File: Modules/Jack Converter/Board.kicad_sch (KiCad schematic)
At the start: 39 parts, among them J1 TS_Jack_3.5mm_Sw, J10 TS_Jack_6.35mm_Sw, J100 IDC_02x08, J11 TS_Jack_3.5mm_Sw, J12 TS_Jack_6.35mm_Sw, J13 TS_Jack_3.5mm_Sw, J14 TS_Jack_6.35mm_Sw, J15 TS_Jack_3.5mm_Sw, J16 TS_Jack_6.35mm_Sw, J17 TS_Jack_3.5mm_Sw, J18 TS_Jack_6.35mm_Sw, J19 TS_Jack_3.5mm_Sw, J2 TS_Jack_6.35mm_Sw, J20 TS_Jack_6.35mm_Sw, J21 TS_Jack_3.5mm_Sw, J22 TS_Jack_6.35mm_Sw, J23 TS_Jack_6.35mm, J3 TS_Jack_3.5mm_Sw, J4 TS_Jack_6.35mm_Sw, J5 TS_Jack_3.5mm_Sw, J6 TS_Jack_6.35mm_Sw, J7 TS_Jack_3.5mm_Sw, J8 TS_Jack_6.35mm_Sw, J9 TS_Jack_3.5mm_Sw, SW1 SW_DPDT, SW2 SW_DPDT, SW3 SW_DPDT, SW4 SW_DPDT

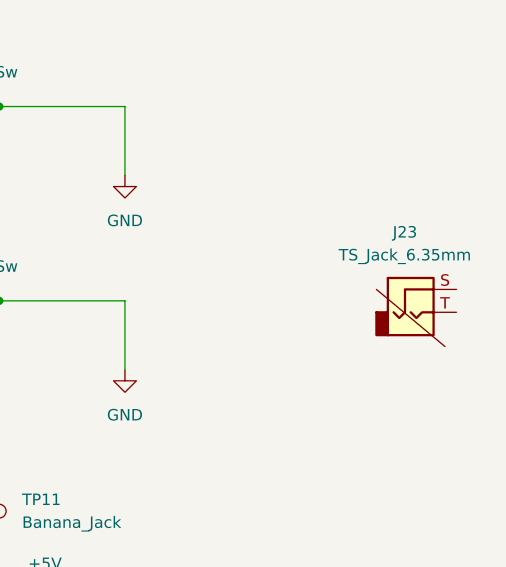
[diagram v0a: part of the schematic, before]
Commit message: Cleaned schematic and downloaded jack mods to footprint library
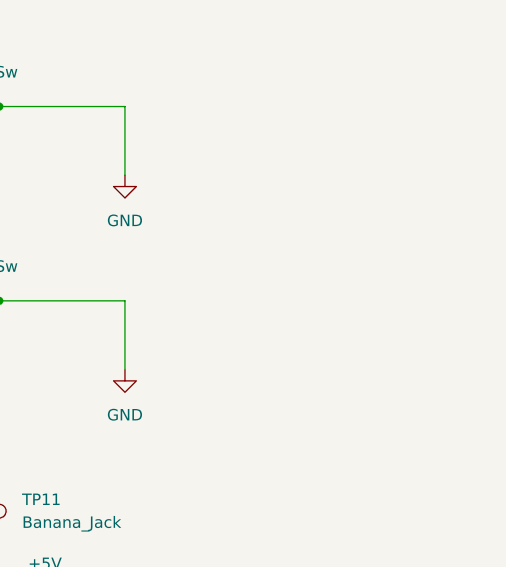
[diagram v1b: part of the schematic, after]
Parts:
- removed J23: TS_Jack_6.35mm, symbol Synth_Stuff:TS_Jack_6.35mm
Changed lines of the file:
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@@
-	)
-	(symbol
-		(lib_id "Synth_Stuff:TS_Jack_6.35mm")
-		(at 251.46 62.23 0)
-		(unit 1)
-		(exclude_from_sim no)
-		(in_bom yes)
-		(on_board yes)
-		(dnp no)
-		(fields_autoplaced yes)
-		(property "Reference" "J23"
-			(at 250.825 53.34 0)
-			(effects
-				(font
-					(size 1.27 1.27)
-				)
-			)
-		)
-		(property "Value" "TS_Jack_6.35mm"
-			(at 250.825 55.88 0)
-			(effects
-				(font
-					(size 1.27 1.27)
-				)
-			)
-		)
-		(property "Footprint" ""
-			(at 251.46 62.23 0)
-			(effects
-				(font
-					(size 1.27 1.27)
-				)
-				(hide yes)
-			)
-		)
-		(property "Datasheet" "~"
-			(at 251.46 62.23 0)
-			(effects
-				(font
-					(size 1.27 1.27)
-				)
-				(hide yes)
-			)
-		)
-		(property "Description" "Audio Jack, 2 Poles (Mono / TS)"
-			(at 251.46 62.23 0)
-			(effects
-				(font
-					(size 1.27 1.27)
-				)
-				(hide yes)
-			)
-		)
-		(pin "T"
-		)
-		(pin "S"
-		)
-		(instances
-			(project "Jack Converter"
-				(path "/b497d75e-0918-4e9c-ae43-36360bc031dc/01b3bf80-fded-40b5-ad81-2678b7ef607a"
-					(reference "J23")
-					(unit 1)
-				)
-			)
-		)
 	)
 	(symbol

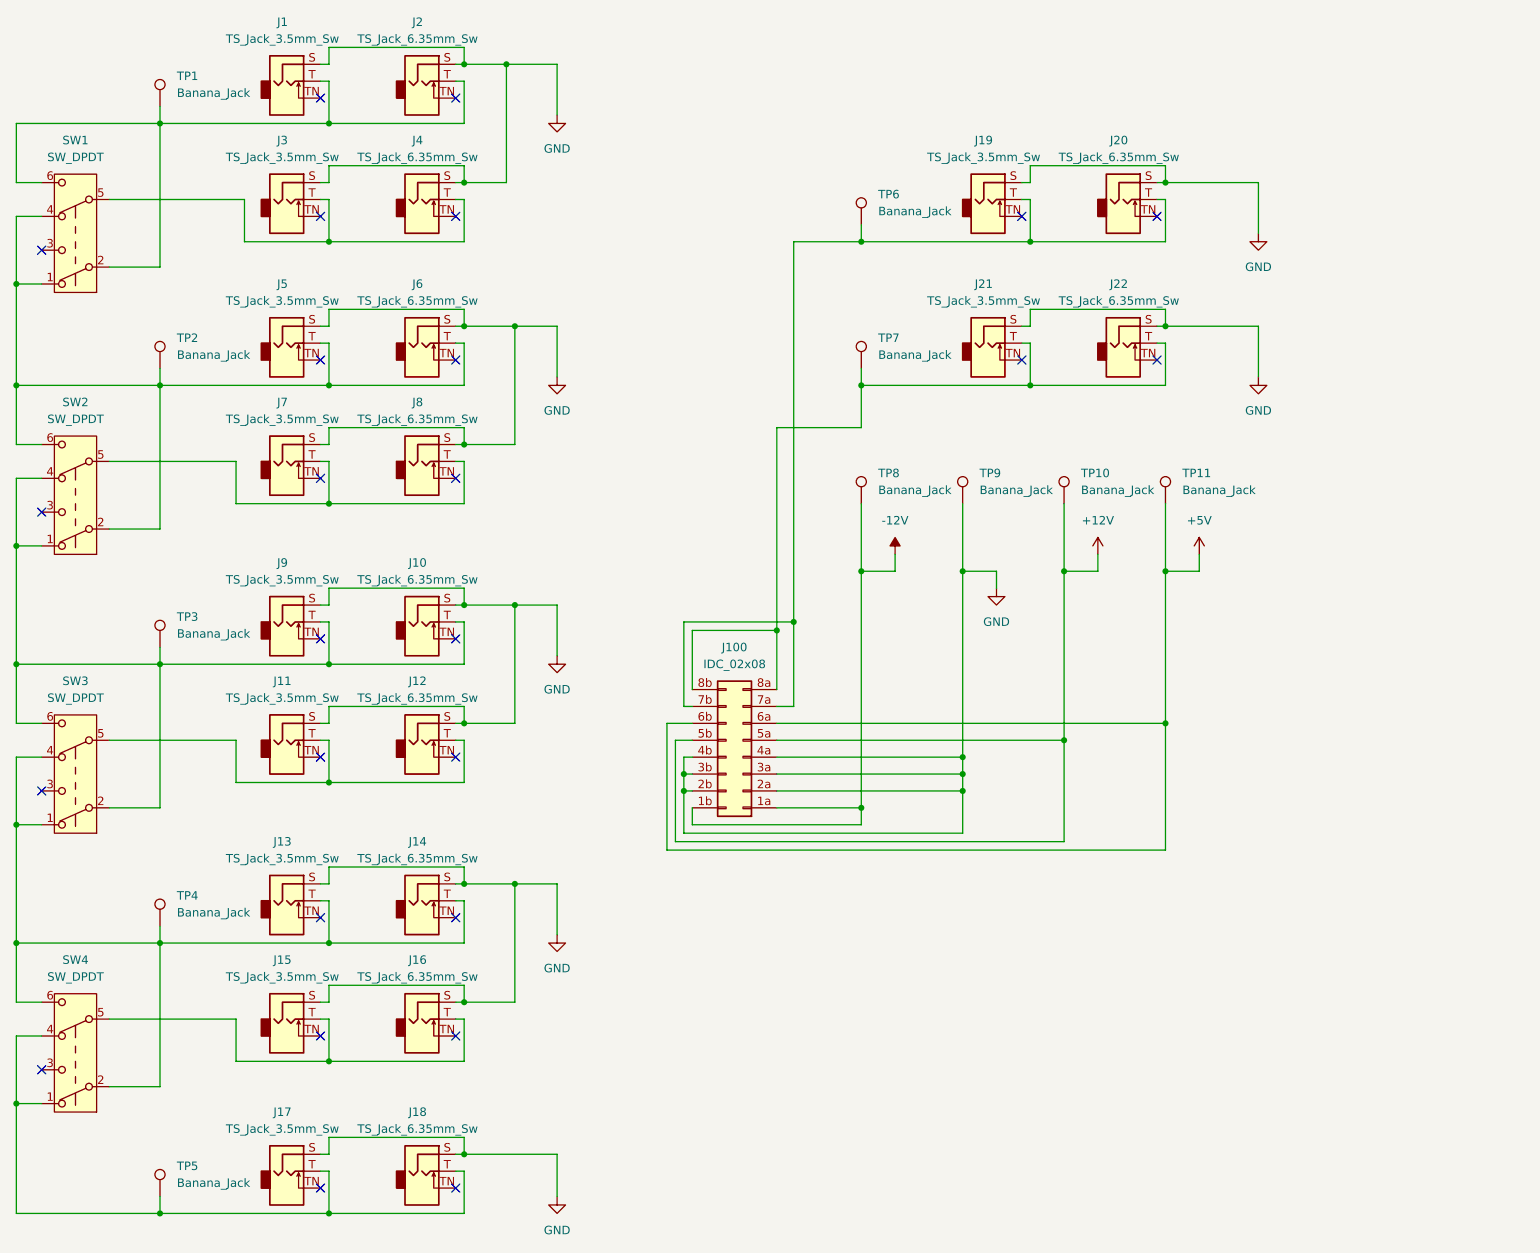
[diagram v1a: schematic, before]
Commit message: Started board PCB creation
Had to remove 2 rows of jacks due to PCB space restriction
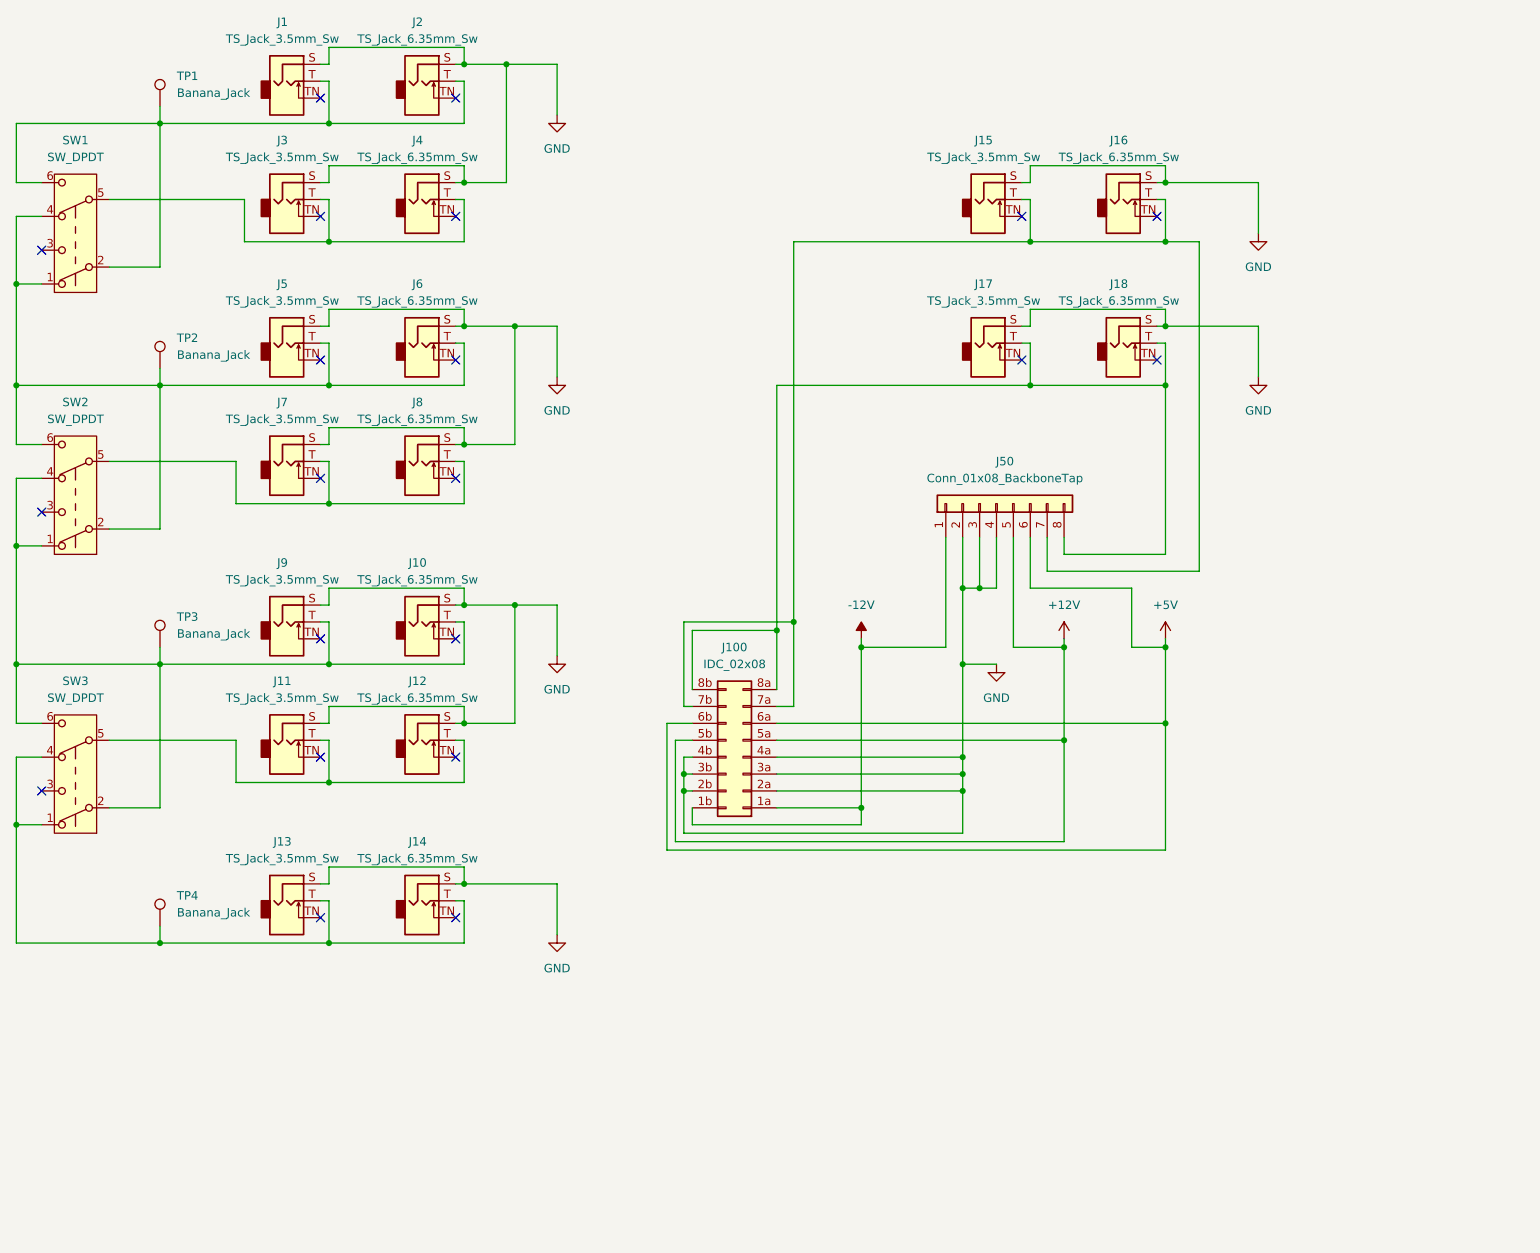
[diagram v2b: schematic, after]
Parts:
- removed J15, J17: TS_Jack_3.5mm_Sw, symbol Synth_Stuff:TS_Jack_3.5mm_Sw
- removed J16, J18: TS_Jack_6.35mm_Sw, symbol Synth_Stuff:TS_Jack_6.35mm_Sw
- removed SW4: SW_DPDT, symbol Synth_Stuff:Switch_DPDT
- removed TP10, TP11, TP5, TP6, TP7, TP8, TP9: Banana_Jack, symbol Synth_Stuff:Banana_Jack
- added J50: Conn_01x08_BackboneTap, Connector_PinHeader_2.54mm:PinHeader_1x08_P2.54mm_Vertical, symbol Synth_Stuff:Conn_01x08_BackboneTap
- J1, J11, J13, J3, J5, J7, J9: footprint (none) -> SynthStuff:AMPHENOL_ACJM-MV35-2S
- J10, J12, J14, J2, J4, J6, J8: footprint (none) -> SynthStuff:CUI_MJ-63052A
- J100: footprint Connector_IDC:IDC-Header_2x08_P2.54mm_Vertical -> SynthStuff:IDC-Header_2x08_P2.54mm_Vertical_Eurorack
- J15: renamed from J19; footprint (none) -> SynthStuff:AMPHENOL_ACJM-MV35-2S
- J16: renamed from J20; footprint (none) -> SynthStuff:CUI_MJ-63052A
- J17: renamed from J21; footprint (none) -> SynthStuff:AMPHENOL_ACJM-MV35-2S
- J18: renamed from J22; footprint (none) -> SynthStuff:CUI_MJ-63052A
- SW1, SW2, SW3: footprint (none) -> SynthStuff:PinHeader_2x03_P2.54mm_Vertical_142536
- TP1, TP2, TP3, TP4: footprint (none) -> Connector_PinHeader_2.54mm:PinHeader_1x01_P2.54mm_Vertical
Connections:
- net +12V: now also J50.5 (Pin_5)
- net +5V: now also J50.6 (Pin_6)
- net -12V: now also J50.1 (Pin_1)
- net GND: now also J50.2 (Pin_2), J50.3 (Pin_3), J50.4 (Pin_4)
- net at J100.7a (Pin_7a), J100.7b (Pin_7b), J15.T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: now also J50.7 (Pin_7)
- net at J100.8a (Pin_8a), J100.8b (Pin_8b), J17.T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: now also J50.8 (Pin_8)
- no-connect marks 26 -> 21

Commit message: Added extra row of jacks, finished positioning
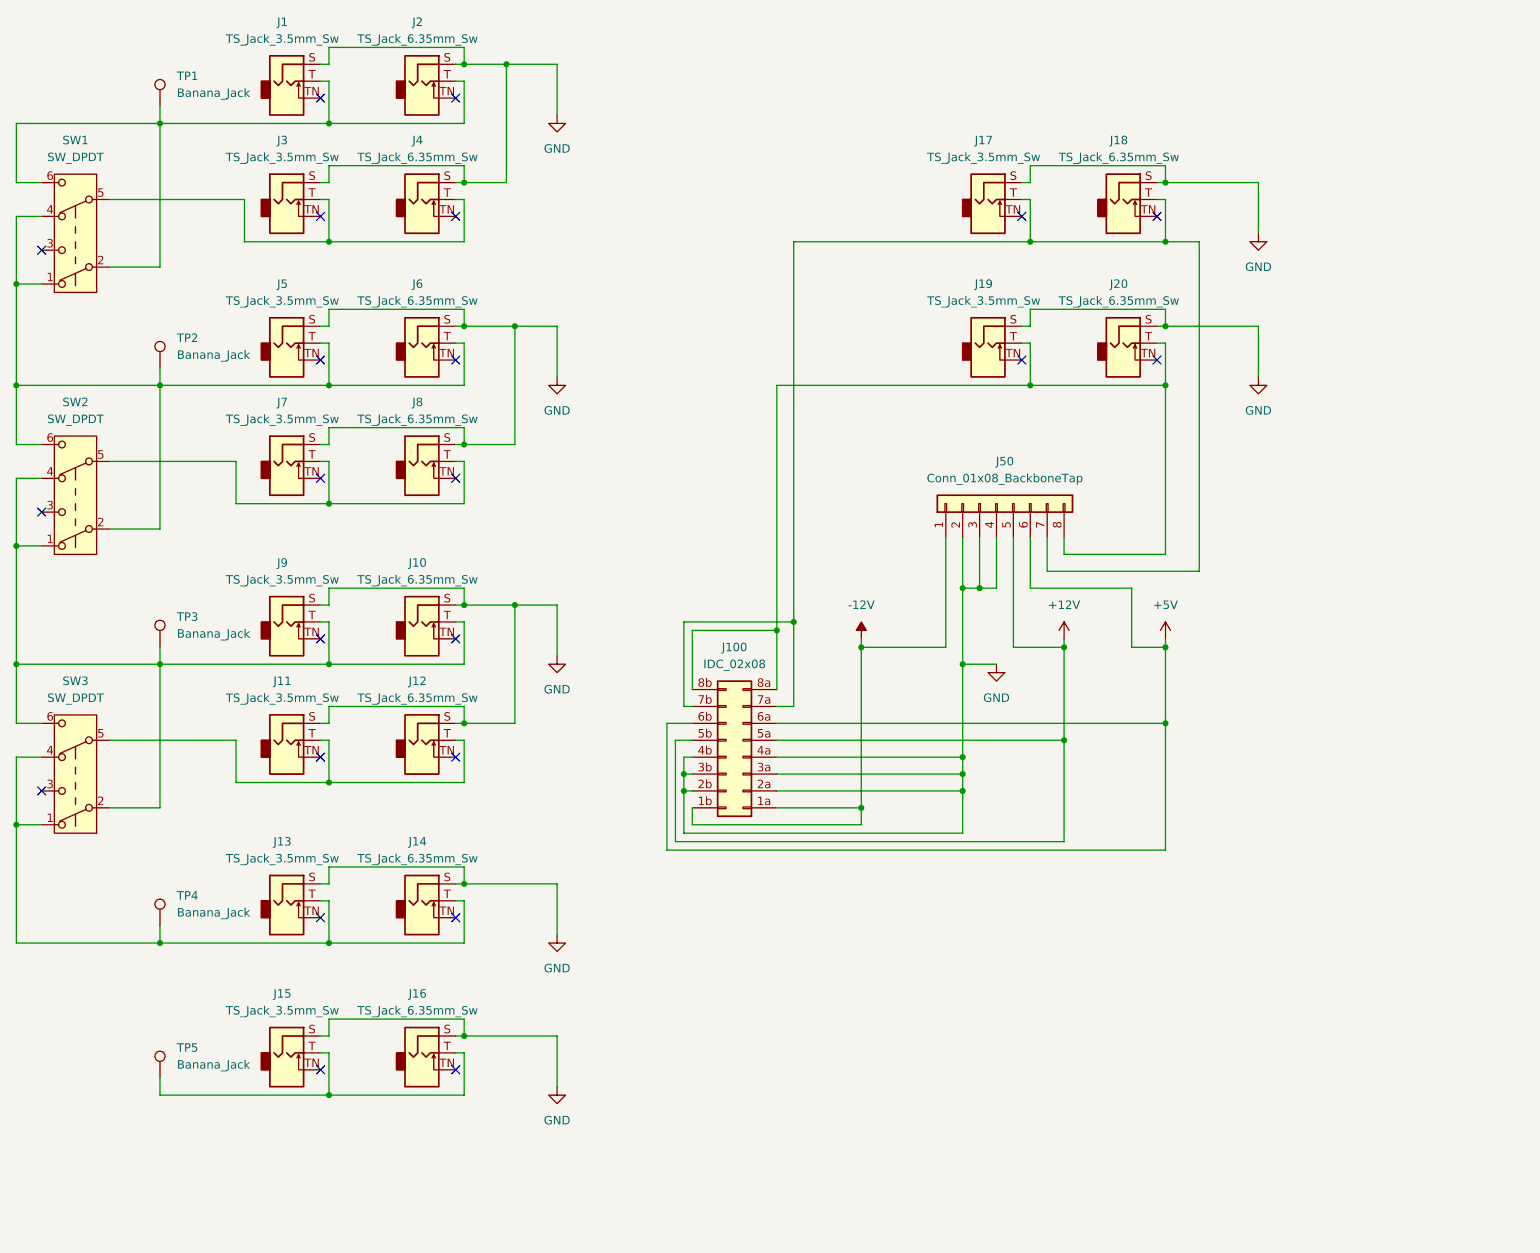
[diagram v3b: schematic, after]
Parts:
- added J15: TS_Jack_3.5mm_Sw, SynthStuff:AMPHENOL_ACJM-MV35-2S, symbol Synth_Stuff:TS_Jack_3.5mm_Sw
- added J16: TS_Jack_6.35mm_Sw, SynthStuff:CUI_MJ-63052A, symbol Synth_Stuff:TS_Jack_6.35mm_Sw
- added TP5: Banana_Jack, Connector_PinHeader_2.54mm:PinHeader_1x01_P2.54mm_Vertical, symbol Synth_Stuff:Banana_Jack
- renumbered J15 to J17, J16 to J18, J17 to J19, J18 to J20
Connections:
- net GND: now also J15.S, J16.S
- new net: J15.T, J16.T, TP5.1
- no-connect marks 21 -> 23

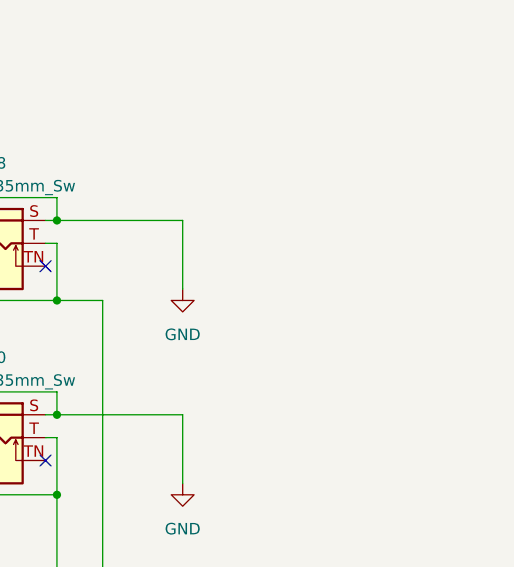
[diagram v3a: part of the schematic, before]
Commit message: Added GND plane and space for switches
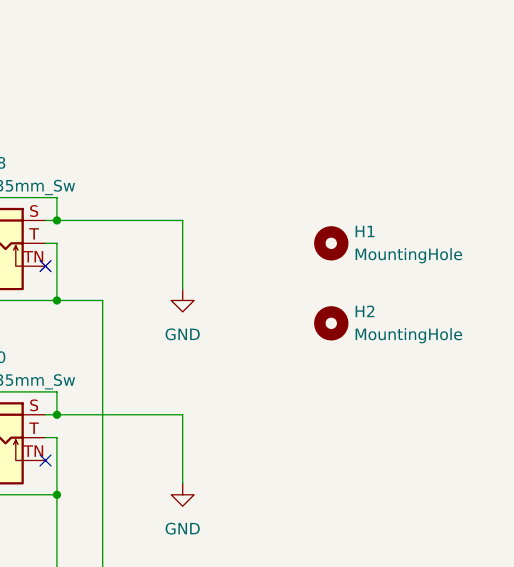
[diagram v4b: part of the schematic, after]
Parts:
- added H1, H2: MountingHole, MountingHole:MountingHole_3.2mm_M3, symbol Mechanical:MountingHole
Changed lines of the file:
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@@
+	)
+	(symbol
+		(lib_id "Mechanical:MountingHole")
+		(at 236.22 50.8 0)
+		(unit 1)
+		(exclude_from_sim yes)
+		(in_bom no)
+		(on_board yes)
+		(dnp no)
+		(fields_autoplaced yes)
+		(property "Reference" "H2"
+			(at 238.76 49.5299 0)
+			(effects
+				(font
+					(size 1.27 1.27)
+				)
+				(justify left)
+			)
+		)
+		(property "Value" "MountingHole"
+			(at 238.76 52.0699 0)
+			(effects
+				(font
+					(size 1.27 1.27)
+				)
+				(justify left)
+			)
+		)
+		(property "Footprint" "MountingHole:MountingHole_3.2mm_M3"
+			(at 236.22 50.8 0)
+			(effects
+				(font
+					(size 1.27 1.27)
+				)
+				(hide yes)
+			)
+		)
+		(property "Datasheet" "~"
+			(at 236.22 50.8 0)
+			(effects
+				(font
+					(size 1.27 1.27)
+				)
+				(hide yes)
+			)
+		)
+		(property "Description" "Mounting Hole without connection"
+			(at 236.22 50.8 0)
+			(effects
+				(font
+					(size 1.27 1.27)
+				)
+				(hide yes)
+			)
+		)
+		(instances
+			(project "Jack Converter"
+				(path "/b497d75e-0918-4e9c-ae43-36360bc031dc/01b3bf80-fded-40b5-ad81-2678b7ef607a"
+					(reference "H2")
+					(unit 1)
+				)
+			)
+		)
 	)
 	(symbol
@@
 					(unit 1)
 				)
+			)
+		)
+	)
+	(symbol
+		(lib_id "Mechanical:MountingHole")
+		(at 236.22 41.91 0)
+		(unit 1)
+		(exclude_from_sim yes)
+		(in_bom no)
+		(on_board yes)
+		(dnp no)
+		(fields_autoplaced yes)
+		(property "Reference" "H1"
+			(at 238.76 40.6399 0)
+			(effects
+				(font
+					(size 1.27 1.27)
+				)
+				(justify left)
+			)
+		)
+		(property "Value" "MountingHole"
+			(at 238.76 43.1799 0)
+			(effects
+				(font
+					(size 1.27 1.27)
+				)
+				(justify left)
+			)
+		)
+		(property "Footprint" "MountingHole:MountingHole_3.2mm_M3"
+			(at 236.22 41.91 0)
+			(effects
+				(font
+					(size 1.27 1.27)
+				)
+				(hide yes)
+			)
+		)
+		(property "Datasheet" "~"
+			(at 236.22 41.91 0)
+			(effects
+				(font
+					(size 1.27 1.27)
+				)
+				(hide yes)
+			)
+		)
+		(property "Description" "Mounting Hole without connection"
+			(at 236.22 41.91 0)
+			(effects
+				(font
+					(size 1.27 1.27)
+				)
+				(hide yes)
+			)
+		)
+		(instances
+			(project "Jack Converter"
+				(path "/b497d75e-0918-4e9c-ae43-36360bc031dc/01b3bf80-fded-40b5-ad81-2678b7ef607a"
+					(reference "H1")
+					(unit 1)
+				)
